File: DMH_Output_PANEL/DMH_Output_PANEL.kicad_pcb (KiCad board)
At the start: 2 copper layers, 50 x 200 mm, 16 parts, among them J0 Panel_GND_Solder_Wire_Pad

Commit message: Front panel design in progress
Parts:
- added H16: Clip L, SynthStuff:MountingHole_LED_3mm, F.Cu at (75.0, 160.2)
- added H17: Clip R, SynthStuff:MountingHole_LED_3mm, F.Cu at (91.5, 160.2)
- moved H11 130.7 mm to (75.0, 171.8)
- moved H10 119.9 mm to (58.5, 190.2)
- moved H9 119.0 mm to (58.5, 171.8)
- moved H14 107.7 mm to (75.0, 100.0)
- moved H12 107.0 mm to (91.5, 171.8)
- moved H15 106.5 mm to (75.0, 62.0)

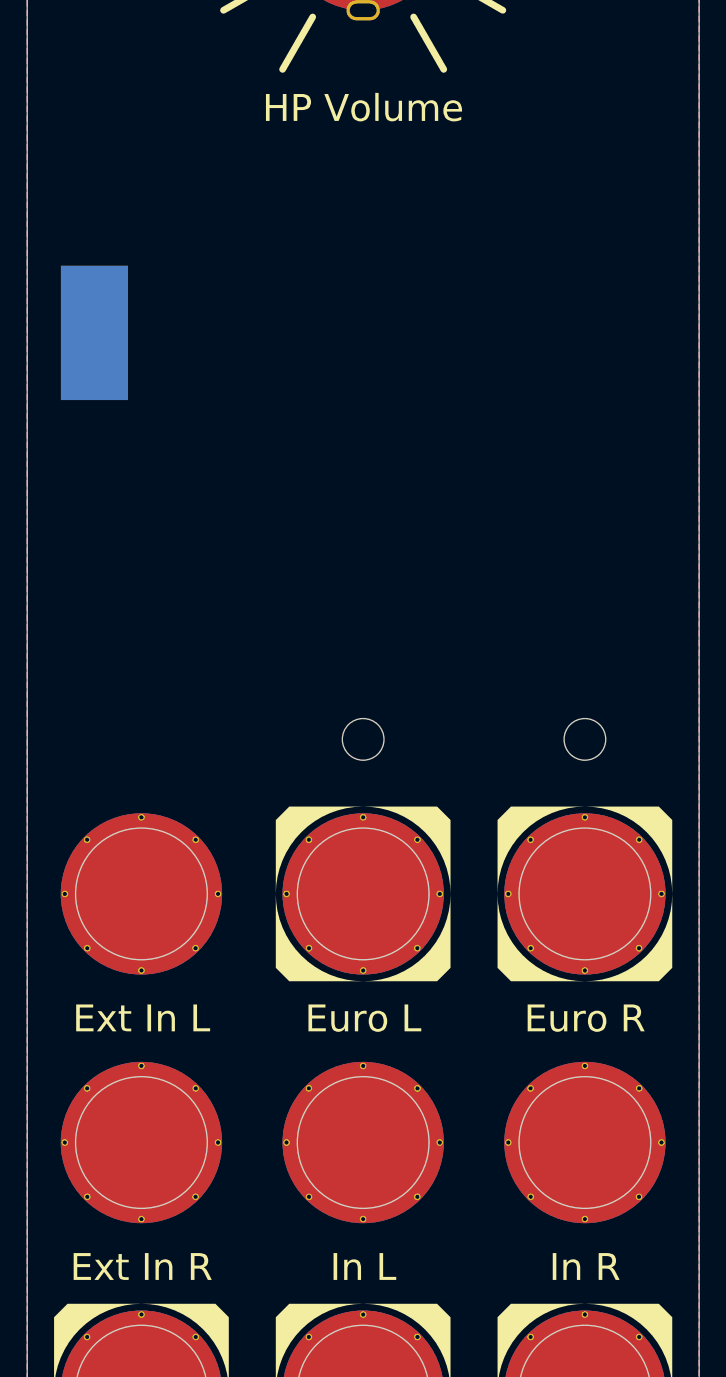
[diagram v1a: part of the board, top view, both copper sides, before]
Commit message: Designed front panel
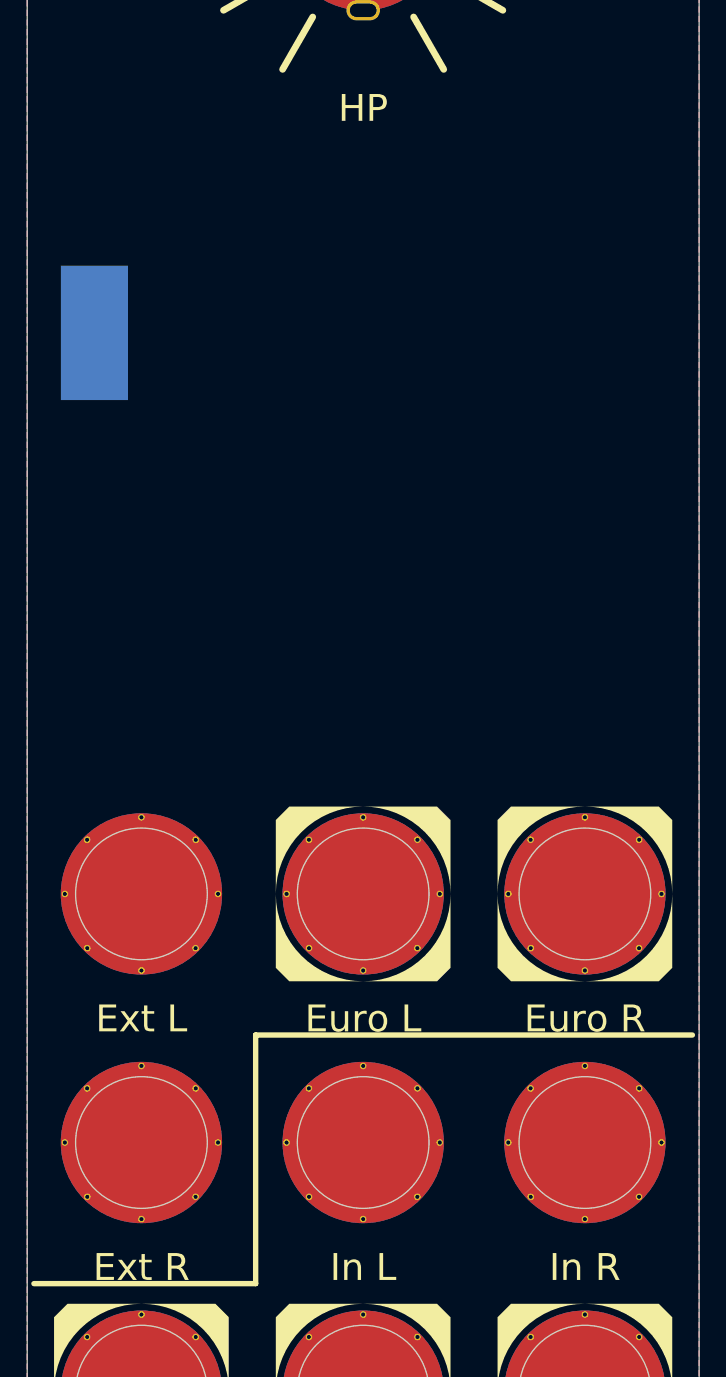
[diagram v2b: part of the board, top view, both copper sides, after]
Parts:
- removed H16: Clip L, SynthStuff:MountingHole_LED_3mm
- removed H17: Clip R, SynthStuff:MountingHole_LED_3mm
- H10: value Ext In R -> Ext R
- H14: value HP Volume -> HP
- H9: value Ext In L -> Ext L

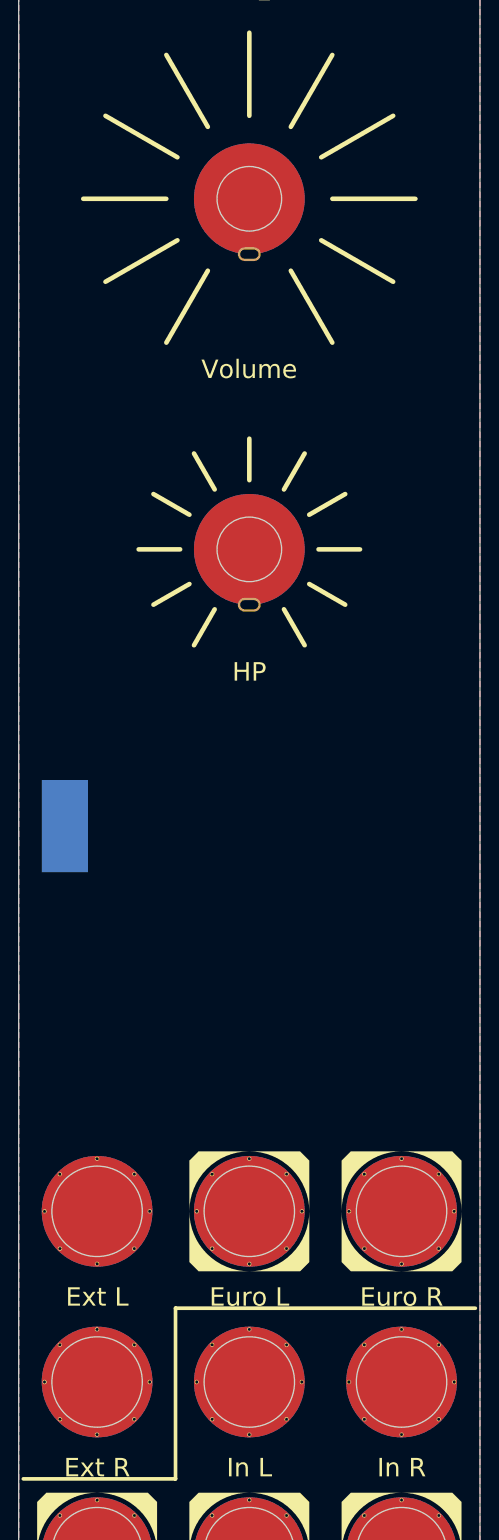
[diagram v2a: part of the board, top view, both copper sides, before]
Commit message: Finished front panel design
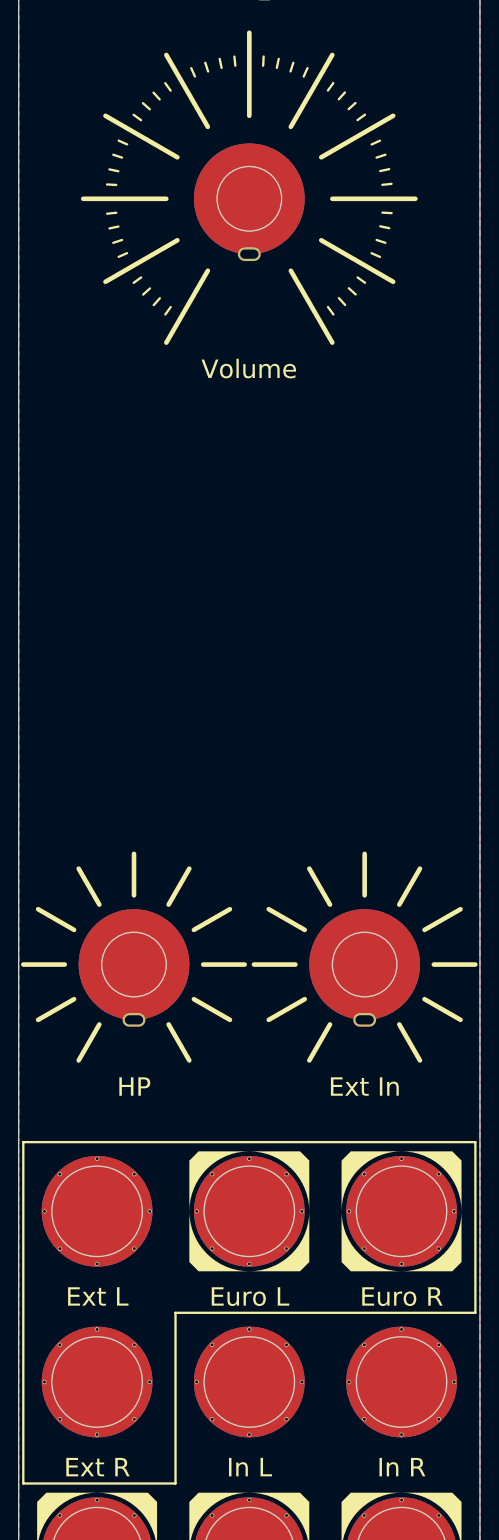
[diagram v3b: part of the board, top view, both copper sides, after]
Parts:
- removed J0: Panel_GND_Solder_Wire_Pad, SynthStuff:Panel_GND_SolderWirePad_5x10mm
- added H18: Ext In, SynthStuff:Pot_Cutout_Tiny, F.Cu at (87.5, 145.0)
- H15: footprint SynthStuff:Pot_Cutout_Medium -> SynthStuff:Pot_Cutout_Medium_v2
- moved H14 46.7 mm to (62.5, 145.0)

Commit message: Schematic in progress
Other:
- board text added: "+3"
- board text added: "+6"
- board text added: "-12"
- board text added: "-15"
- board text added: "-18"
- board text added: "-21"
- board text added: "-3"
- board text added: "-6"
- board text added: "-9"
- board text added: "0"

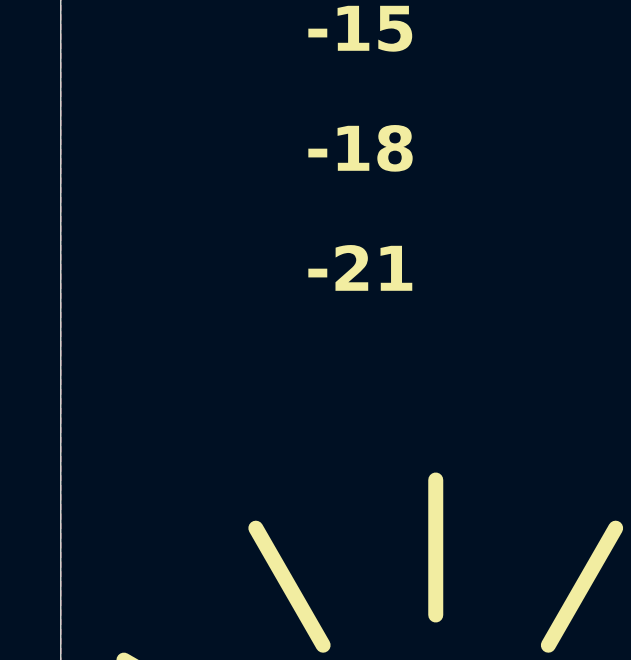
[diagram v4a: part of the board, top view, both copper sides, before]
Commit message: Centralized library
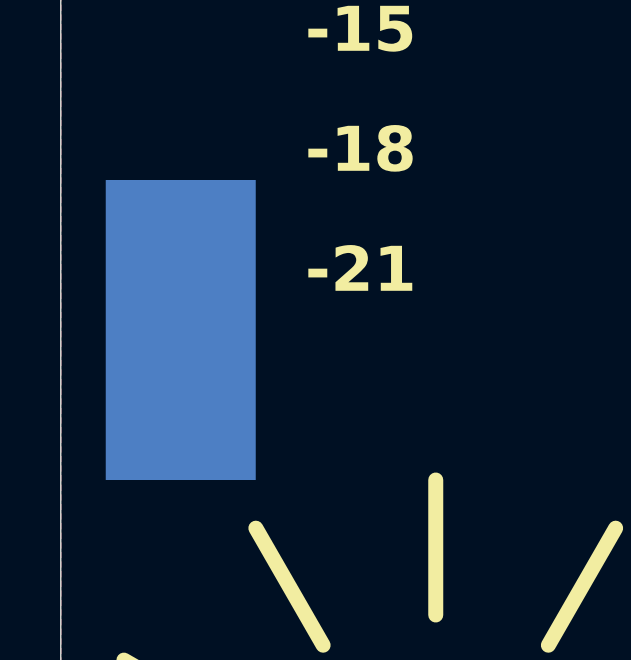
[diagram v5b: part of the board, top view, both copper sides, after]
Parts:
- added J0: Panel_GND_Solder_Wire_Pad, SynthStuff:Panel_GND_SolderWirePad_5x10mm, B.Cu at (54.0, 128.0)
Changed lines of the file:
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@@
 		)
 		(embedded_fonts no)
-		(model "${KIPRJMOD}/Libraries/SynthStuff/3D_models/c-5-1437624-3-a-3d.stp"
+		(model "${KIPRJMOD}/../Libraries/SynthStuff/3D_models/c-5-1437624-3-a-3d.stp"
 			(offset
 				(xyz 0 0 14.5)
@@
 			)
 		)
-		(model "${KIPRJMOD}/Libraries/SynthStuff/3D_models/ALPHA-RD901F-40.step"
+		(model "${KIPRJMOD}/../Libraries/SynthStuff/3D_models/ALPHA-RD901F-40.step"
 			(hide yes)
 			(offset
@@
 		)
 		(embedded_fonts no)
-		(model "${KIPRJMOD}/Libraries/SynthStuff/3D_models/User Library-jack-4.STEP"
+		(model "${KIPRJMOD}/../Libraries/SynthStuff/3D_models/User Library-jack-4.STEP"
 			(offset
 				(xyz 0 0 -3)
@@
 		)
 		(embedded_fonts no)
-		(model "${KIPRJMOD}/Libraries/SynthStuff/3D_models/User Library-jack-4.STEP"
+		(model "${KIPRJMOD}/../Libraries/SynthStuff/3D_models/User Library-jack-4.STEP"
 			(offset
 				(xyz 0 0 -3)
@@
 		)
 		(embedded_fonts no)
-		(model "${KIPRJMOD}/Libraries/SynthStuff/3D_models/User Library-jack-4.STEP"
+		(model "${KIPRJMOD}/../Libraries/SynthStuff/3D_models/User Library-jack-4.STEP"
 			(offset
 				(xyz 0 0 -3)
@@
 		)
 		(embedded_fonts no)
-		(model "${KIPRJMOD}/Libraries/SynthStuff/3D_models/User Library-jack-4.STEP"
+		(model "${KIPRJMOD}/../Libraries/SynthStuff/3D_models/User Library-jack-4.STEP"
 			(offset
 				(xyz 0 0 -3)
@@
 		)
 		(embedded_fonts no)
-		(model "${KIPRJMOD}/Libraries/SynthStuff/3D_models/User Library-jack-4.STEP"
+		(model "${KIPRJMOD}/../Libraries/SynthStuff/3D_models/User Library-jack-4.STEP"
 			(offset
 				(xyz 0 0 -3)
@@
 		)
 		(embedded_fonts no)
-		(model "${KIPRJMOD}/Libraries/SynthStuff/3D_models/c-5-1437624-0-a-3d.stp"
+		(model "${KIPRJMOD}/../Libraries/SynthStuff/3D_models/c-5-1437624-0-a-3d.stp"
 			(offset
 				(xyz 0 0 12)
@@
 			)
 		)
-		(model "${KIPRJMOD}/Libraries/SynthStuff/3D_models/ALPHA-RD901F-40.step"
+		(model "${KIPRJMOD}/../Libraries/SynthStuff/3D_models/ALPHA-RD901F-40.step"
 			(hide yes)
 			(offset
@@
 		)
 		(embedded_fonts no)
-		(model "${KIPRJMOD}/Libraries/SynthStuff/3D_models/User Library-jack-4.STEP"
+		(model "${KIPRJMOD}/../Libraries/SynthStuff/3D_models/User Library-jack-4.STEP"
 			(offset
 				(xyz 0 0 -3)
@@
 		)
 		(embedded_fonts no)
-		(model "${KIPRJMOD}/Libraries/SynthStuff/3D_models/User Library-jack-4.STEP"
+		(model "${KIPRJMOD}/../Libraries/SynthStuff/3D_models/User Library-jack-4.STEP"
 			(offset
 				(xyz 0 0 -3)
@@
 		)
 		(embedded_fonts no)
-		(model "${KIPRJMOD}/Libraries/SynthStuff/3D_models/User Library-jack-4.STEP"
+		(model "${KIPRJMOD}/../Libraries/SynthStuff/3D_models/User Library-jack-4.STEP"
 			(offset
 				(xyz 0 0 -3)
@@
 		)
 		(embedded_fonts no)
-		(model "${KIPRJMOD}/Libraries/SynthStuff/3D_models/c-5-1437624-0-a-3d.stp"
+		(model "${KIPRJMOD}/../Libraries/SynthStuff/3D_models/c-5-1437624-0-a-3d.stp"
 			(offset
 				(xyz 0 0 12)
@@
 			)
 		)
-		(model "${KIPRJMOD}/Libraries/SynthStuff/3D_models/ALPHA-RD901F-40.step"
+		(model "${KIPRJMOD}/../Libraries/SynthStuff/3D_models/ALPHA-RD901F-40.step"
 			(hide yes)
 			(offset
@@
 		)
 		(embedded_fonts no)
-		(model "${KIPRJMOD}/Libraries/SynthStuff/3D_models/User Library-jack-4.STEP"
+		(model "${KIPRJMOD}/../Libraries/SynthStuff/3D_models/User Library-jack-4.STEP"
 			(offset
 				(xyz 0 0 -3)
@@
 		)
 	)
+	(footprint "SynthStuff:Panel_GND_SolderWirePad_5x10mm"
+		(layer "B.Cu")
+		(at 54 128 180)
+		(descr "Wire Pad, Square, SMD Pad,  5mm x 10mm,")
+		(tags "MesurementPoint Square SMDPad 5mmx10mm ")
+		(property "Reference" "J0"
+			(at 0 3.81 0)
+			(layer "B.SilkS")
+			(hide yes)
+			(effects
+				(font
+					(size 1 1)
+					(thickness 0.15)
+				)
+				(justify mirror)
+			)
+		)
+		(property "Value" "Panel_GND_Solder_Wire_Pad"
+			(at 0 -6.35 0)
+			(layer "B.Fab")
+			(hide yes)
+			(effects
+				(font
+					(size 1 1)
+					(thickness 0.15)
+				)
+				(justify mirror)
+			)
+		)
+		(property "Datasheet" "~"
+			(at 0 0 0)
+			(unlocked yes)
+			(layer "B.Fab")
+			(hide yes)
+			(effects
+				(font
+					(size 1.27 1.27)
+					(thickness 0.15)
+				)
+				(justify mirror)
+			)
+		)
+		(property "Description" "Solder pad to allow connection between PCB and Front Panel"
+			(at 0 0 0)
+			(unlocked yes)
+			(layer "B.Fab")
+			(hide yes)
+			(effects
+				(font
+					(size 1.27 1.27)
+					(thickness 0.15)
+				)
+				(justify mirror)
+			)
+		)
+		(property "Function" "GND"
+			(at 0 -6.4 0)
+			(layer "B.SilkS")
+			(effects
+				(font
+					(size 1 1)
+					(thickness 0.2)
+					(bold yes)
+				)
+				(justify mirror)
+			)
+		)
+		(property ki_fp_filters "Connector*:*_1x??_*")
+		(sheetname "/")
+		(sheetfile "DMH_Output_PANEL.kicad_sch")
+		(zone_connect 1)
+		(attr smd exclude_from_pos_files exclude_from_bom dnp)
+		(fp_line
+			(start 2.75 5.25)
+			(end -2.75 5.25)
+			(stroke
+				(width 0.05)
+				(type solid)
+			)
+			(layer "B.CrtYd")
+		)
+		(fp_line
+			(start 2.75 -5.25)
+			(end 2.75 5.25)
+			(stroke
+				(width 0.05)
+				(type solid)
+			)
+			(layer "B.CrtYd")
+		)
+		(fp_line
+			(start -2.75 5.25)
+			(end -2.75 -5.25)
+			(stroke
+				(width 0.05)
+				(type solid)
+			)
+			(layer "B.CrtYd")
+		)
+		(fp_line
+			(start -2.75 -5.25)
+			(end 2.75 -5.25)
+			(stroke
+				(width 0.05)
+				(type solid)
+			)
+			(layer "B.CrtYd")
+		)
+		(fp_text user "${REFERENCE}"
+			(at 0 0 0)
+			(layer "B.Fab")
+			(effects
+				(font
+					(size 1 1)
+					(thickness 0.15)
+				)
+				(justify mirror)
+			)
+		)
+		(pad "1" smd rect
+			(at 0 0 180)
+			(size 5 10)
+			(layers "B.Cu" "B.Mask" "B.Paste")
+			(net 1 "GND")
+			(pinfunction "Pin_1")
+			(pintype "power_out")
+		)
+		(embedded_fonts no)
+	)
 	(gr_line

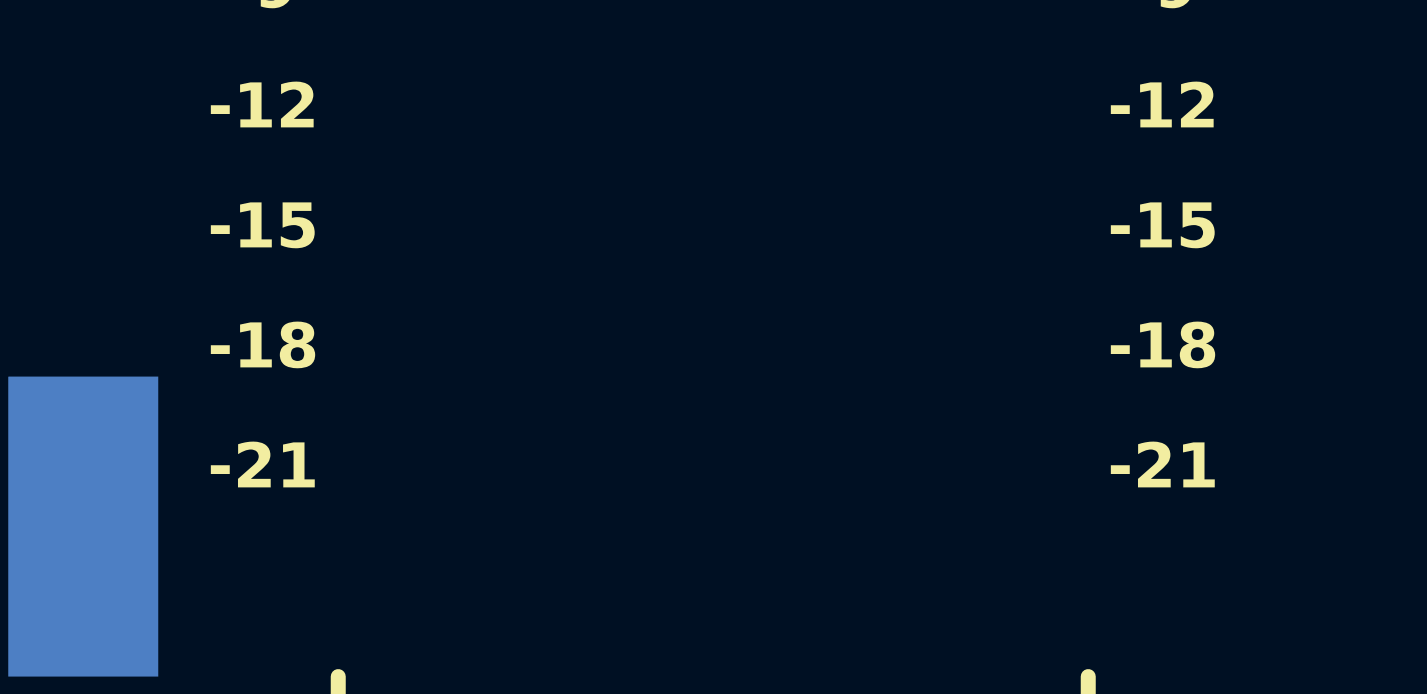
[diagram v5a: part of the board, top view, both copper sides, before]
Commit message: Starting design of Controls PCB
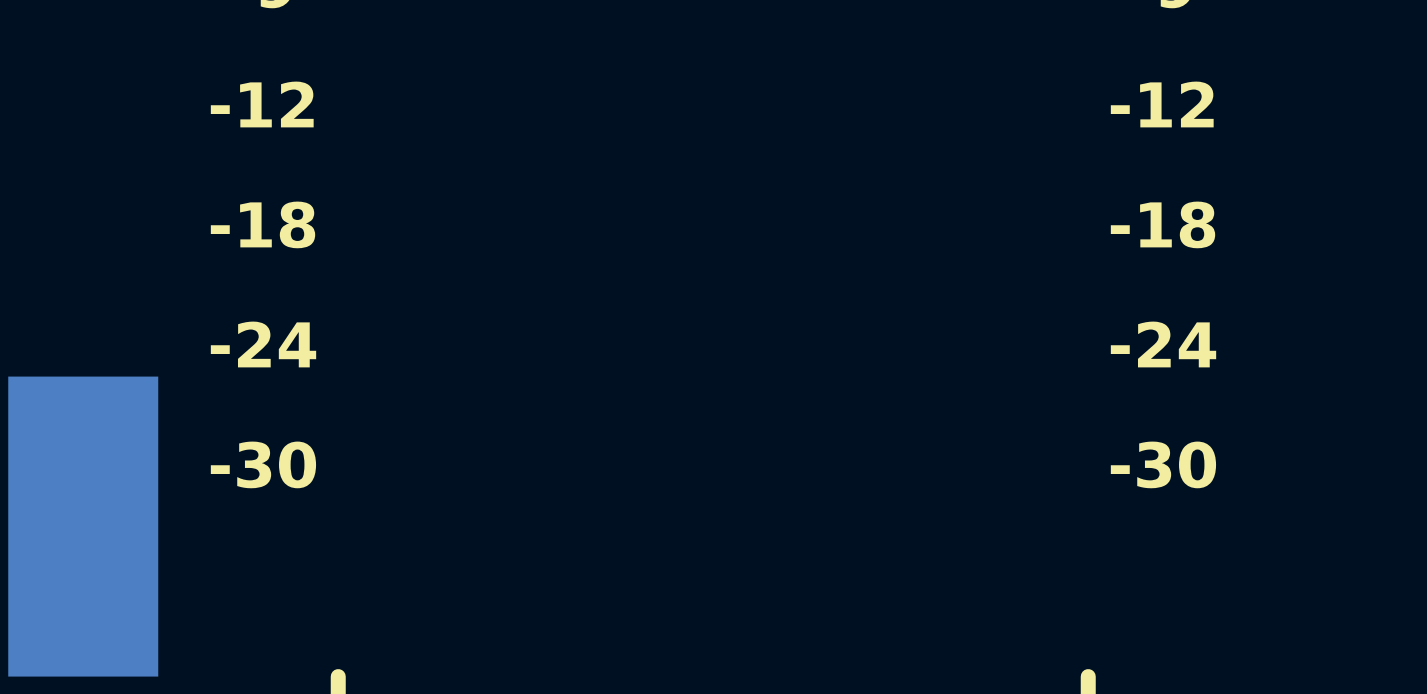
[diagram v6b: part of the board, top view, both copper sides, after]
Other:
- board text added: "-24"
- board text added: "-30"
- board text removed: "-15"
- board text removed: "-21"
